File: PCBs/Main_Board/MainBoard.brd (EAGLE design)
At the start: 100 x 80 mm, 24 parts

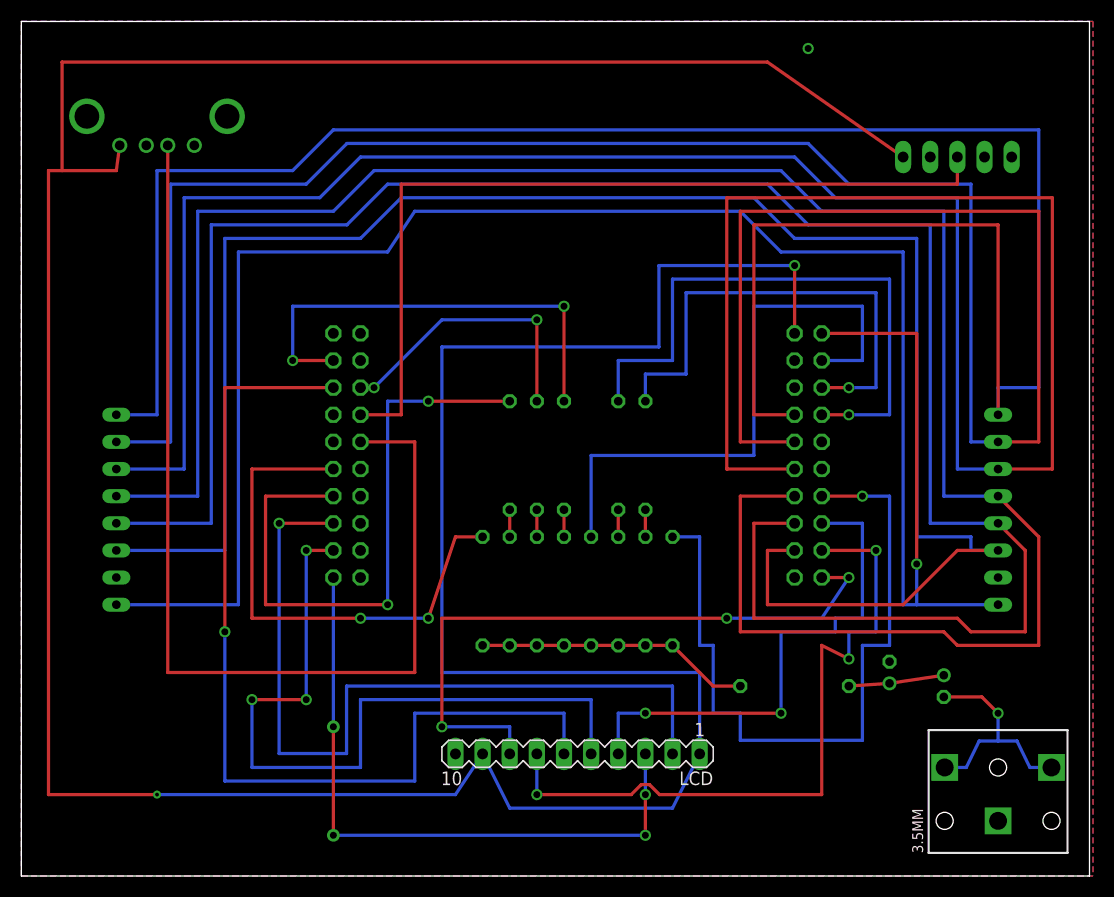
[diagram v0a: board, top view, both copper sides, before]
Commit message: Created main board layout
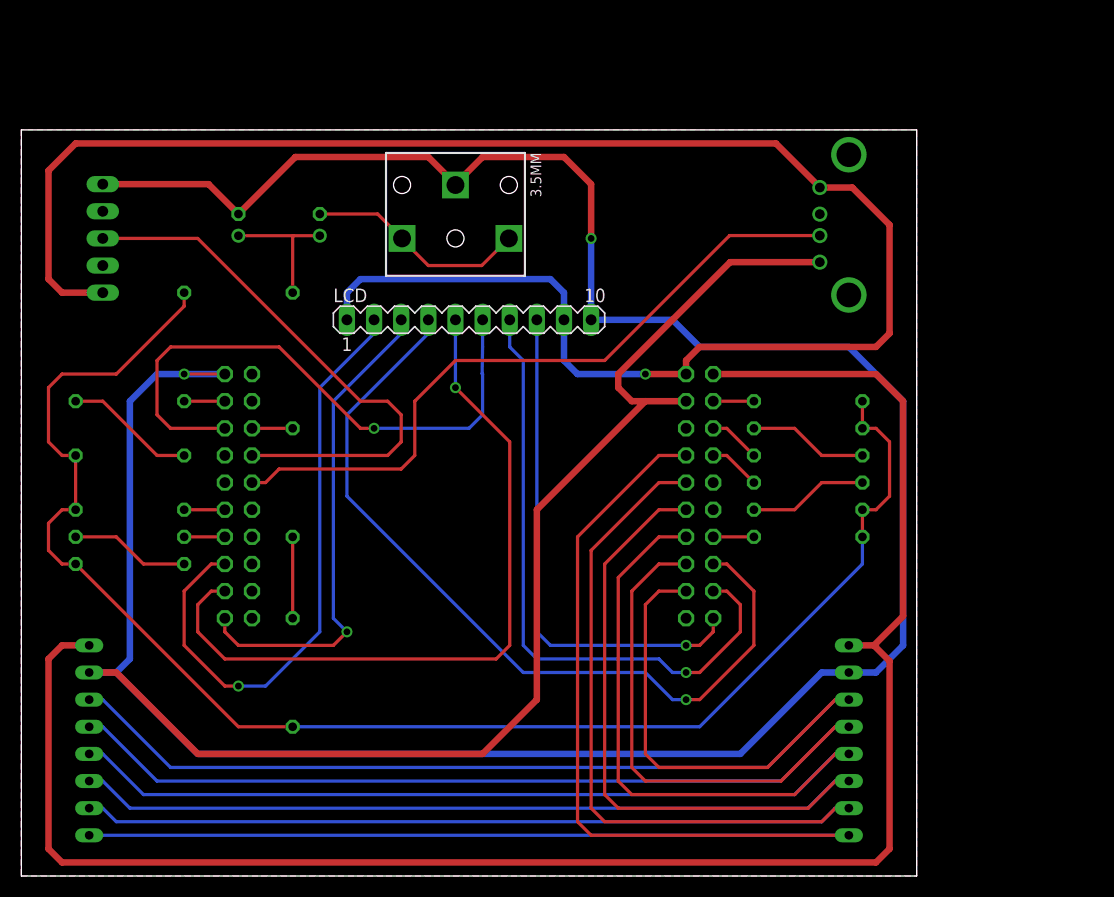
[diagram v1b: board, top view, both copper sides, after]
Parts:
- removed INPUT_L: (no value), con-lsta:FE08W
- added INPUT_R.: (no value), con-lsta:FE08W
- moved USB_B 80.4 mm to (7.62, 59.7), turned to 270 degrees
- moved C2 74.0 mm to (20.3, 61.0)
- moved C1 72.6 mm to (27.9, 61.0), turned to 90 degrees
- moved 3.5MM 70.9 mm to (40.6, 59.7), turned to 270 degrees
- moved USB_A 65.6 mm to (77.5, 61.0), turned to 0 degrees
- moved R14 63.8 mm to (20.3, 54.6)
- moved R6 42.6 mm to (10.2, 39.4), turned to 180 degrees
- moved LCD 41.9 mm to (41.9, 52.1), turned to 0 degrees
- moved R11 41.0 mm to (10.2, 44.5), turned to 180 degrees
- moved R9 36.4 mm to (10.2, 31.8), turned to 180 degrees
- moved R2 35.7 mm to (10.2, 29.2), turned to 180 degrees
- moved R1 33.9 mm to (10.2, 34.3), turned to 180 degrees
- moved R3 27.0 mm to (73.7, 44.5), turned to 0 degrees
- moved INPUT_R 25.7 mm to (77.5, 12.7)
- moved R5 24.1 mm to (25.4, 19.1)
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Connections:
- net GND: now also INPUT_R..2, INPUT_R.7; no longer INPUT_L.7, INPUT_R.2
- net IN_0: now also INPUT_R..8, INPUT_R.1; no longer INPUT_L.1, INPUT_R.8
- net IN_1: now also INPUT_R..7, INPUT_R.2; no longer INPUT_L.2, INPUT_R.7
- net IN_2: now also INPUT_R..6, INPUT_R.3; no longer INPUT_L.3, INPUT_R.6
- net IN_3: now also INPUT_R..5, INPUT_R.4; no longer INPUT_L.4, INPUT_R.5
- net IN_4: now also INPUT_R..4, INPUT_R.5; no longer INPUT_L.5, INPUT_R.4
- net IN_5: now also INPUT_R..3, INPUT_R.6; no longer INPUT_L.6, INPUT_R.3
- net VCC_3.3: now also INPUT_R..1, INPUT_R.8; no longer INPUT_L.8, INPUT_R.1
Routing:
- net GND: track 0.00 -> 354.2 mm, vias 1 -> 2
- net VCC_5: track 339.5 -> 172.5 mm, vias 2 -> 1
- net DAC_OUT: track 25.7 -> 144.1 mm
- net IN_2: track 229.2 -> 129.0 mm
- net IN_1: track 214.0 -> 133.0 mm
- net IN_3: track 200.8 -> 124.9 mm
- net IN_4: track 191.4 -> 120.9 mm
- net IN_0: track 203.5 -> 137.0 mm
- net DAC_4: track 68.6 -> 3.81 mm, vias 1 -> 0
- net IN_5: track 175.4 -> 116.9 mm
- net DAC_6: track 58.4 -> 3.81 mm, vias 2 -> 0
- net DAC_5: track 55.9 -> 3.81 mm
- net DAC_1: track 55.9 -> 4.86 mm, vias 1 -> 0
- net DAC_7: track 48.7 -> 3.81 mm, vias 2 -> 0
- net DAC_0: track 45.7 -> 4.86 mm, vias 1 -> 0
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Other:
- board size 100 x 80 mm -> 83.8 x 69.8 mm
